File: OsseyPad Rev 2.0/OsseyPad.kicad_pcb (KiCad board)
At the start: 2 copper layers, 157 x 148 mm, 85 parts, among them SW1 Rotary_Encoder_Switch, U1 Elite-C

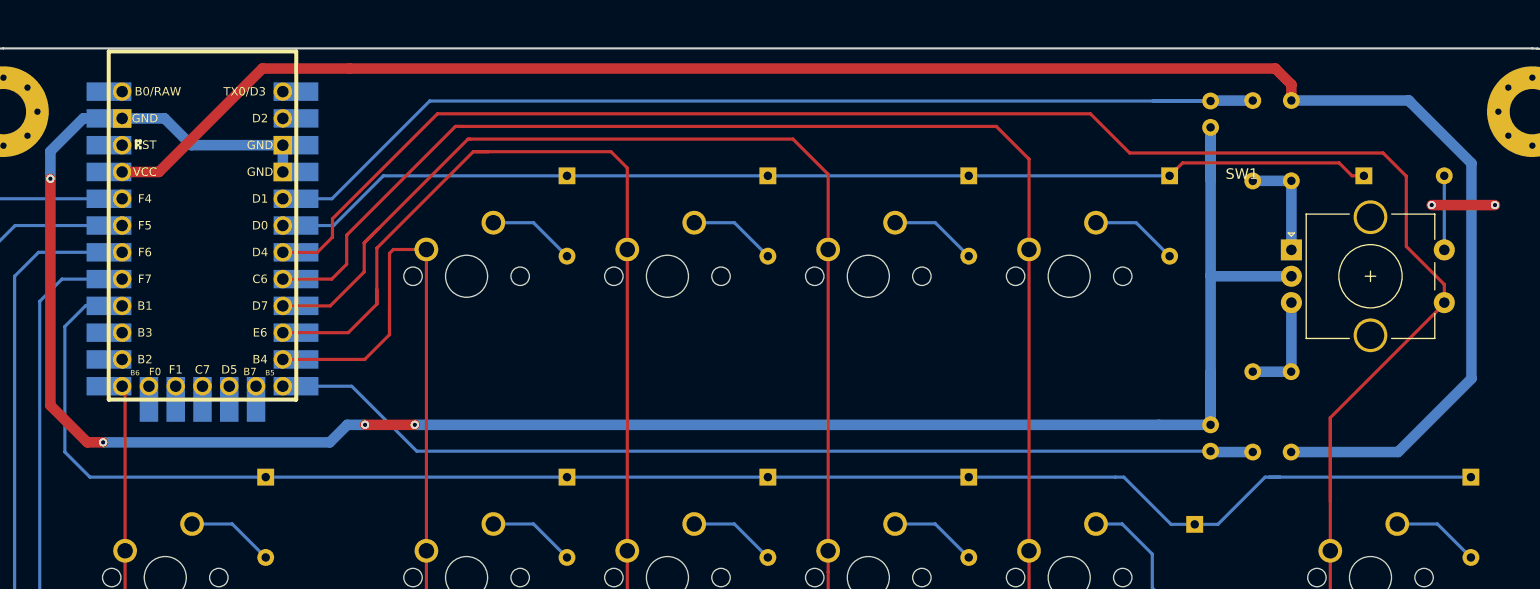
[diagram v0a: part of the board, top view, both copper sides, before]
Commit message: Updated the pcb and case.
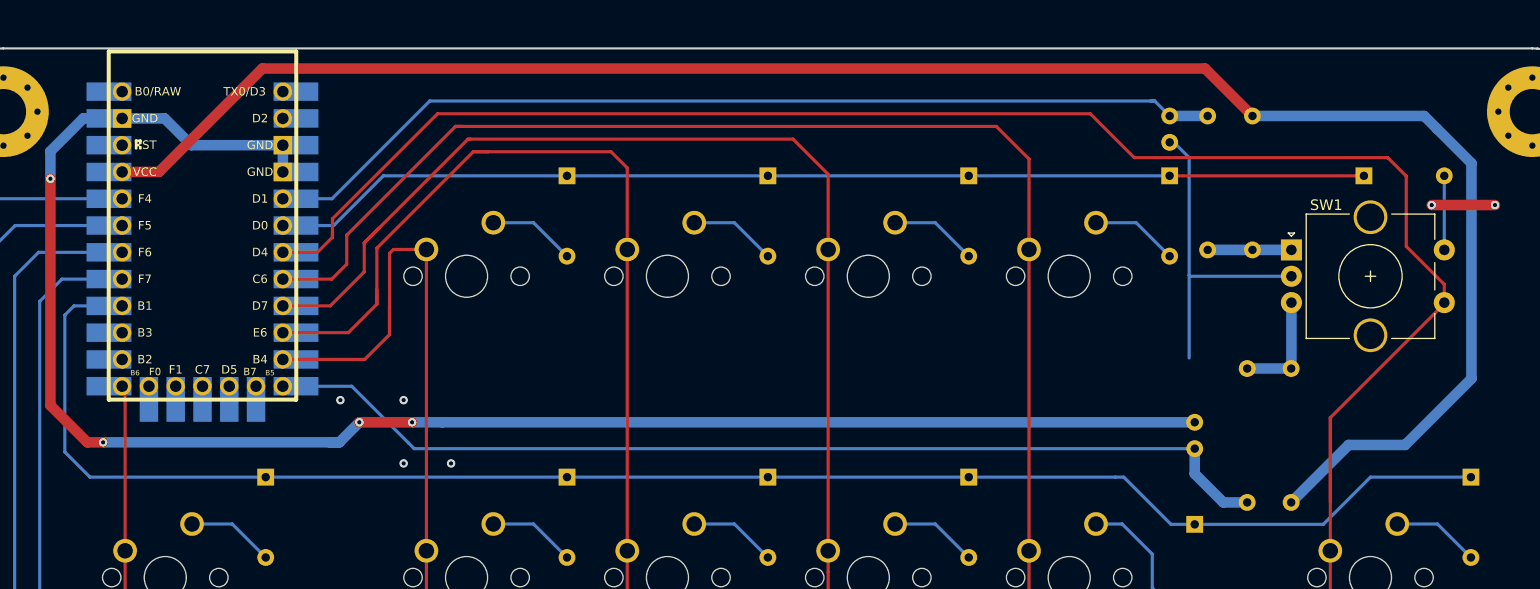
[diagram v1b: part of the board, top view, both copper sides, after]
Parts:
- R1, R2, R3, R4: footprint Resistor_THT:R_Axial_DIN0207_L6.3mm_D2.5mm_P7.62mm_Horizontal -> Resistor_THT:R_Axial_DIN0309_L9.0mm_D3.2mm_P12.70mm_Horizontal
- moved R3 7.82 mm to (201.2, 92.8)
- moved R2 4.78 mm to (209.2, 116.7)
- moved C2 4.13 mm to (197.7, 80.0)
- moved R1 3.97 mm to (205.5, 80.0)
- moved C1 1.52 mm to (200.0, 111.6)
- moved R4 0.61 mm to (205.0, 104.0)
- moved G*** 0.10 mm to (202.5, 212.6)
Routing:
- net GND: track 213.9 -> 199.4 mm, vias 6 -> 10
- net ENC_1_A: track 100.1 -> 91.3 mm
- net ENC_1_B: track 93.4 -> 96.2 mm
- net Net-(R1-Pad2): track 10.2 -> 7.94 mm
- net ROW0: track 104.2 -> 103.2 mm
- net +5V: track 177.3 -> 178.1 mm

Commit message: Updated the pcb and made the production files.
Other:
- board text added: "Designed by Osku Väyrynen 24/2/2021 Rev 2.0"
- board text removed: "Designed by Osku Väyrynen 10/2/2021 Rev 2.0"
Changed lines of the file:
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@@
       (viasonmask false)
       (mode 1)
-      (useauxorigin false)
+      (useauxorigin true)
       (hpglpennumber 1)
       (hpglpenspeed 20)
@@
     (property "Sheetname" "")
     (attr through_hole)
-    (fp_text reference "SW1" (at -4.19375 -6.75) (layer "F.SilkS")
+    (fp_text reference "SW1" (at -4.19375 -6.75) (layer "Cmts.User")
       (effects (font (size 1 1) (thickness 0.15)))
     )
@@
     (effects (font (size 1 1) (thickness 0.25)))
   )
-  (gr_text "Designed by Osku Väyrynen\n10/2/2021\nRev 2.0\n" (at 159.55 104.4) (layer "B.SilkS")
+  (gr_text "Designed by Osku Väyrynen\n24/2/2021\nRev 2.0\n" (at 159.55 104.4) (layer "B.SilkS")
     (effects (font (size 2 2) (thickness 0.4)) (justify mirror))
   )
